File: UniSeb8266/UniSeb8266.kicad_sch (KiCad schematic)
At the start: 30 parts, among them IC1 WEMOS-D1-MINI, IC2 GY-BME280-3.3, IC3 LM1117IMPX-, IC4 MCP23008SS, IC5 RT9400, IC6 AMS5915, J1 22-?-0327-2031, X1 AK500/2, X2 AK500/2, X3 233-503, X5 233-504, X61 JST-XH-05-PIN-LONG-PAD, X7 0446200002, X8 233-508

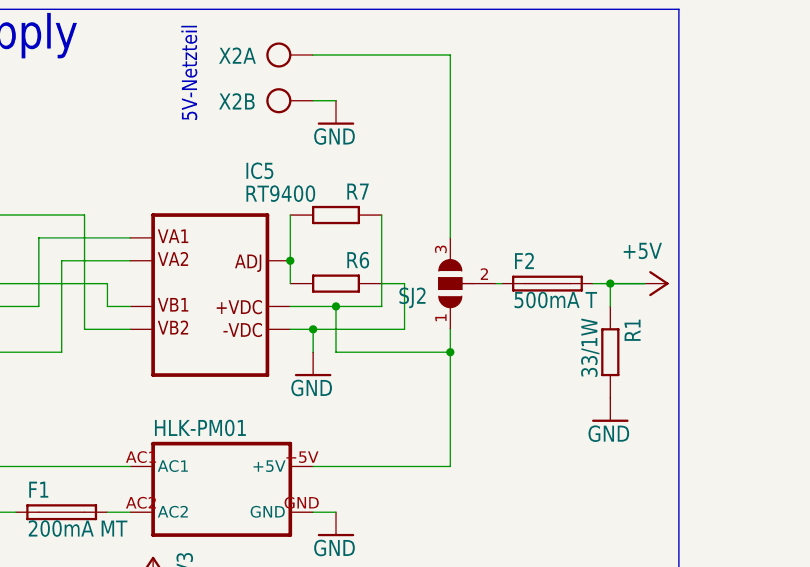
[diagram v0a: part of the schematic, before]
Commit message: changed name of SJ2 -> SJ1
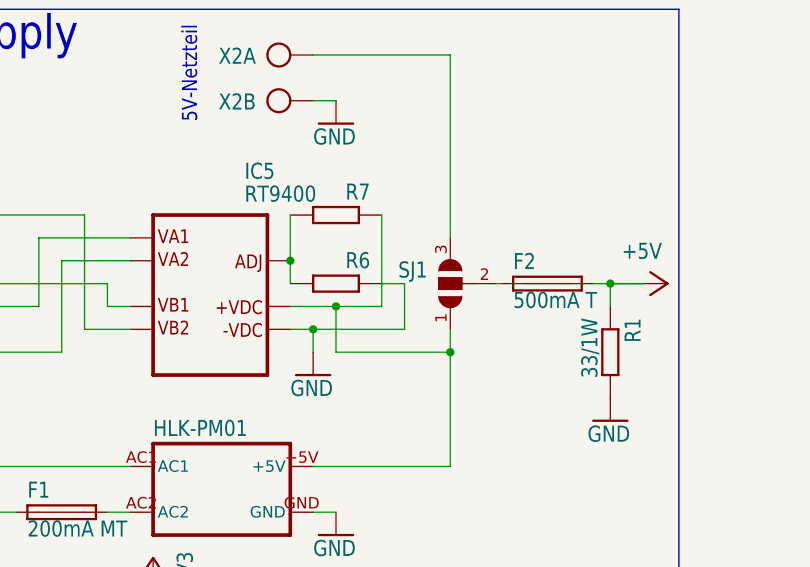
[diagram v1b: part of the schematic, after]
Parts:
- renumbered SJ2 to SJ1
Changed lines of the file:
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@@
   (symbol (lib_id "UniSeb8266-eagle-import:SJ2W") (at 96.52 53.34 180) (unit 1)
     (in_bom yes) (on_board yes) (dnp no)
-    (property "Reference" "SJ2" (at 93.98 53.721 0)
+    (property "Reference" "SJ1" (at 93.98 50.8 0)
       (effects (font (size 1.778 1.5113)) (justify left bottom))
     )
@@
       (project "UniSeb8266"
         (path "/7f528db3-ace1-4a57-b27a-eb0bf0e98f2a"
-          (reference "SJ2") (unit 1)
+          (reference "SJ1") (unit 1)
         )
       )

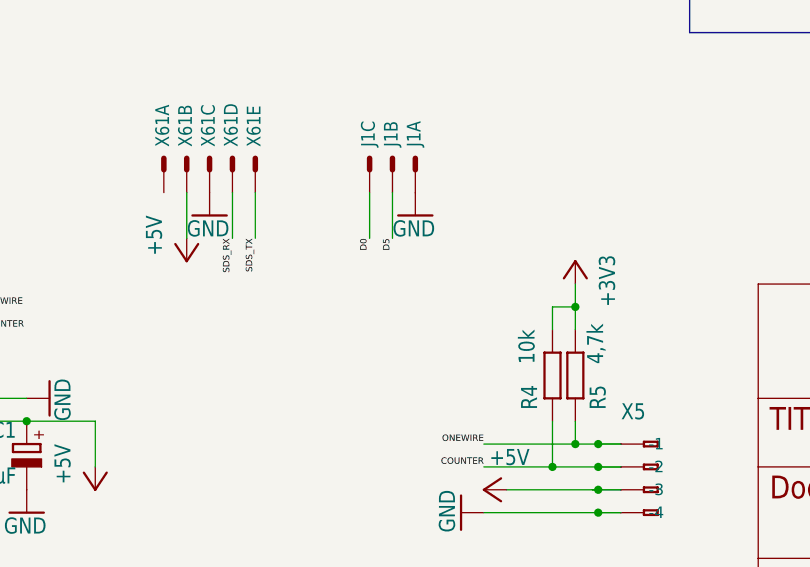
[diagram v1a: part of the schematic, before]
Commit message: added SJ2 to change pin-2 usage of "Molex KK 254" connector (3.3V or D5)
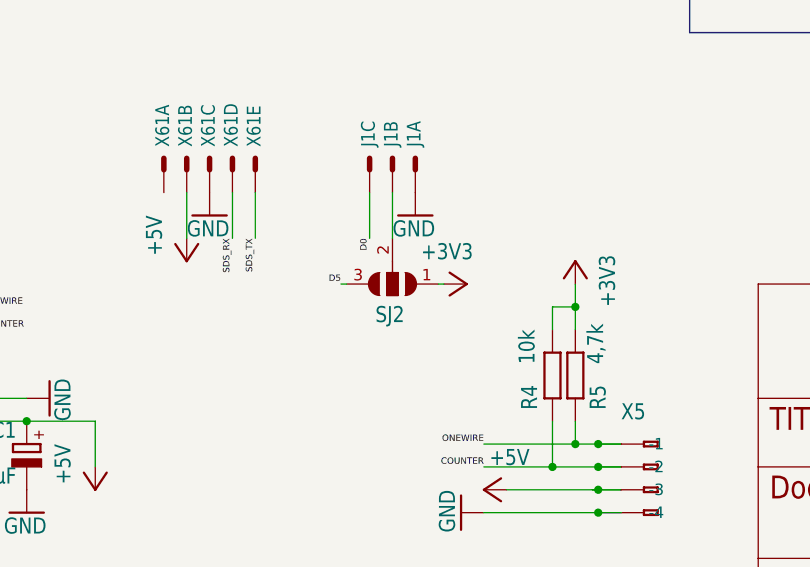
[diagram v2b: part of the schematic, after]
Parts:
- added SJ2: SJ2W, UniSeb8266:SJ_2, symbol UniSeb8266-eagle-import:SJ2W
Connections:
- net +3V3: now also SJ2.1
- net D5: now also SJ2.3; no longer J1.2 (S)
- new net: J1.2 (S), SJ2.2
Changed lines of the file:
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@@
     (stroke (width 0.1524) (type solid))
+  )
+  (wire (pts (xy 139.7 152.4) (xy 139.7 157.48))
+    (stroke (width 0) (type default))
   )
   (wire (pts (xy 157.48 177.8) (xy 157.48 182.88))
@@
     (stroke (width 0.1524) (type solid))
   )
+  (wire (pts (xy 133.985 162.56) (xy 134.62 162.56))
+    (stroke (width 0) (type default))
+  )
   (wire (pts (xy 81.28 33.02) (xy 83.82 33.02))
     (stroke (width 0.1524) (type solid))
@@
     (stroke (width 0.1524) (type solid))
   )
-  (wire (pts (xy 139.7 152.4) (xy 139.7 157.48))
-    (stroke (width 0.1524) (type solid))
-  )
   (wire (pts (xy 99.06 177.8) (xy 106.68 177.8))
     (stroke (width 0.1524) (type solid))
@@
   (wire (pts (xy 243.84 99.06) (xy 251.46 99.06))
     (stroke (width 0.1524) (type solid))
+  )
+  (wire (pts (xy 145.415 162.56) (xy 144.78 162.56))
+    (stroke (width 0) (type default))
   )
   (wire (pts (xy 220.98 71.12) (xy 220.98 66.04))
@@
     (effects (font (size 0.7112 0.7112)) (justify right bottom))
   )
-  (label "D5" (at 139.7 157.48 270) (fields_autoplaced)
+  (label "D5" (at 133.985 162.56 180) (fields_autoplaced)
     (effects (font (size 0.7112 0.7112)) (justify right bottom))
   )
@@
     )
   )
+  (symbol (lib_id "UniSeb8266-eagle-import:SJ2W") (at 139.7 162.56 270) (unit 1)
+    (in_bom yes) (on_board yes) (dnp no)
+    (property "Reference" "SJ2" (at 137.795 167.005 90)
+      (effects (font (size 1.778 1.5113)) (justify left bottom))
+    )
+    (property "Value" "SJ2W" (at 137.795 165.1 0)
+      (effects (font (size 1.778 1.5113)) (justify left bottom) hide)
+    )
+    (property "Footprint" "UniSeb8266:SJ_2" (at 139.7 162.56 0)
+      (effects (font (size 1.27 1.27)) hide)
+    )
+    (property "Datasheet" "" (at 139.7 162.56 0)
+      (effects (font (size 1.27 1.27)) hide)
+    )
+    (pin "1")
+    (pin "2")
+    (pin "3")
+    (instances
+      (project "UniSeb8266"
+        (path "/7f528db3-ace1-4a57-b27a-eb0bf0e98f2a"
+          (reference "SJ2") (unit 1)
+        )
+      )
+    )
+  )
   (symbol (lib_id "UniSeb8266-eagle-import:R-EU_R1206") (at 157.48 172.72 90) (unit 1)
     (in_bom yes) (on_board yes) (dnp no)
@@
         )
       )
+    )
+  )
+  (symbol (lib_id "UniSeb8266-eagle-import:+3V3") (at 147.955 162.56 270) (unit 1)
+    (in_bom yes) (on_board yes) (dnp no)
+    (property "Reference" "#+3V02" (at 147.955 162.56 0)
+      (effects (font (size 1.27 1.27)) hide)
+    )
+    (property "Value" "+3V3" (at 142.875 160.02 90)
+      (effects (font (size 1.778 1.5113)) (justify left bottom))
+    )
+    (property "Footprint" "" (at 147.955 162.56 0)
+      (effects (font (size 1.27 1.27)) hide)
+    )
+    (property "Datasheet" "" (at 147.955 162.56 0)
+      (effects (font (size 1.27 1.27)) hide)
+    )
+    (pin "1")
+    (instances
+      (project "UniSeb8266"
+        (path "/7f528db3-ace1-4a57-b27a-eb0bf0e98f2a"
+          (reference "#+3V02") (unit 1)
+        )
+      )

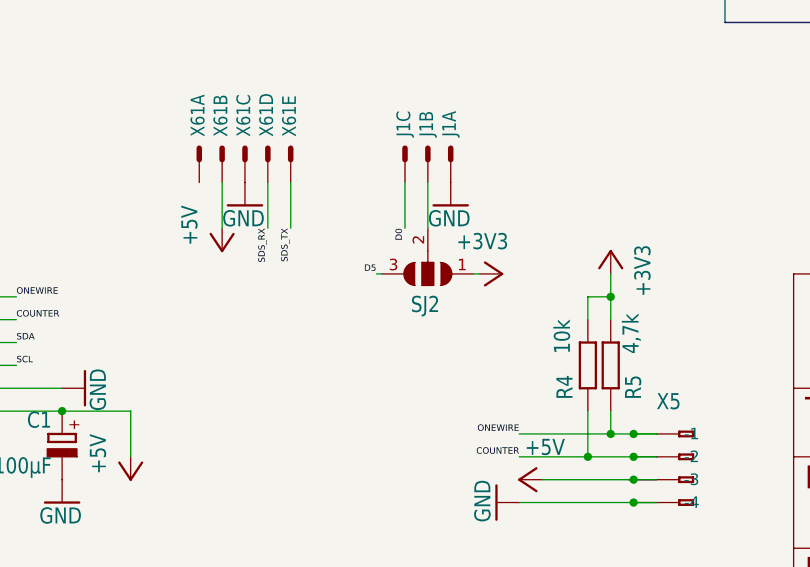
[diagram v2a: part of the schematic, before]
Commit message: added R2 pullup for pin3 of J1
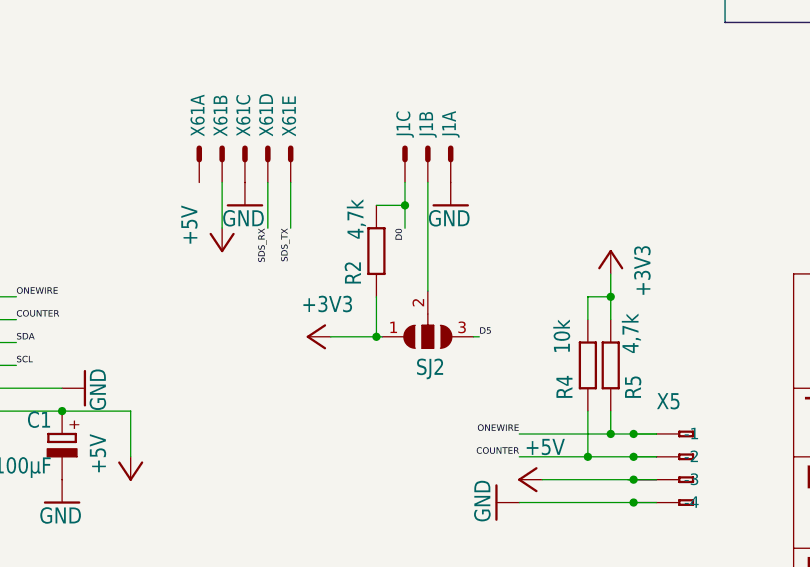
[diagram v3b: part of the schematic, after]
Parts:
- added R2: 4,7k, Resistor_SMD:R_0603_1608Metric, symbol UniSeb8266-eagle-import:R-EU_R1206
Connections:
- net +3V3: now also R2.1
- net D0: now also R2.2
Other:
- moved on the sheet: SJ2
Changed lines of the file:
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@@
   (junction (at 246.38 83.82) (diameter 0) (color 0 0 0 0)
   )
+  (junction (at 137.16 154.94) (diameter 0) (color 0 0 0 0)
+  )
   (junction (at 160.02 165.1) (diameter 0) (color 0 0 0 0)
   )
@@
   (junction (at 43.18 60.96) (diameter 0) (color 0 0 0 0)
   )
+  (junction (at 133.985 169.545) (diameter 0) (color 0 0 0 0)
+  )
   (junction (at 162.56 185.42) (diameter 0) (color 0 0 0 0)
   )
@@
     (stroke (width 0.1524) (type solid))
   )
-  (wire (pts (xy 137.16 152.4) (xy 137.16 157.48))
+  (wire (pts (xy 137.16 152.4) (xy 137.16 154.94))
     (stroke (width 0.1524) (type solid))
   )
@@
     (stroke (width 0.1524) (type solid))
   )
+  (wire (pts (xy 137.16 154.94) (xy 137.16 157.48))
+    (stroke (width 0.1524) (type solid))
+  )
   (wire (pts (xy 152.4 185.42) (xy 162.56 185.42))
     (stroke (width 0.1524) (type solid))
@@
     (stroke (width 0.1524) (type solid))
   )
+  (wire (pts (xy 133.985 154.94) (xy 137.16 154.94))
+    (stroke (width 0) (type default))
+  )
   (wire (pts (xy 256.54 53.34) (xy 256.54 50.8))
     (stroke (width 0.1524) (type solid))
@@
     (stroke (width 0.1524) (type solid))
   )
-  (wire (pts (xy 139.7 152.4) (xy 139.7 157.48))
+  (wire (pts (xy 139.7 152.4) (xy 139.7 164.465))
     (stroke (width 0) (type default))
   )
@@
     (stroke (width 0.1524) (type solid))
   )
+  (wire (pts (xy 133.985 169.545) (xy 134.62 169.545))
+    (stroke (width 0) (type default))
+  )
   (wire (pts (xy 243.84 93.98) (xy 256.54 93.98))
     (stroke (width 0.1524) (type solid))
@@
     (stroke (width 0.1524) (type solid))
   )
-  (wire (pts (xy 133.985 162.56) (xy 134.62 162.56))
+  (wire (pts (xy 145.415 169.545) (xy 144.78 169.545))
     (stroke (width 0) (type default))
   )
@@
     (stroke (width 0.1524) (type solid))
   )
+  (wire (pts (xy 133.985 165.1) (xy 133.985 169.545))
+    (stroke (width 0) (type default))
+  )
   (wire (pts (xy 43.18 60.96) (xy 53.34 60.96))
     (stroke (width 0.1524) (type solid))
@@
     (stroke (width 0.1524) (type solid))
   )
-  (wire (pts (xy 145.415 162.56) (xy 144.78 162.56))
+  (wire (pts (xy 128.905 169.545) (xy 133.985 169.545))
     (stroke (width 0) (type default))
   )
@@
     (effects (font (size 0.7112 0.7112)) (justify right bottom))
   )
-  (label "D5" (at 133.985 162.56 180) (fields_autoplaced)
-    (effects (font (size 0.7112 0.7112)) (justify right bottom))
+  (label "D5" (at 145.415 169.545 0) (fields_autoplaced)
+    (effects (font (size 0.7112 0.7112)) (justify left bottom))
   )
   (label "EXP-INT" (at 53.34 170.18 180) (fields_autoplaced)
@@
     )
   )
-  (symbol (lib_id "UniSeb8266-eagle-import:SJ2W") (at 139.7 162.56 270) (unit 1)
-    (in_bom yes) (on_board yes) (dnp no)
-    (property "Reference" "SJ2" (at 137.795 167.005 90)
-      (effects (font (size 1.778 1.5113)) (justify left bottom))
-    )
-    (property "Value" "SJ2W" (at 137.795 165.1 0)
+  (symbol (lib_id "UniSeb8266-eagle-import:SJ2W") (at 139.7 169.545 90) (mirror x) (unit 1)
+    (in_bom yes) (on_board yes) (dnp no)
+    (property "Reference" "SJ2" (at 141.605 173.99 90)
+      (effects (font (size 1.778 1.5113)) (justify left bottom))
+    )
+    (property "Value" "SJ2W" (at 141.605 172.085 0)
       (effects (font (size 1.778 1.5113)) (justify left bottom) hide)
     )
-    (property "Footprint" "UniSeb8266:SJ_2" (at 139.7 162.56 0)
-      (effects (font (size 1.27 1.27)) hide)
-    )
-    (property "Datasheet" "" (at 139.7 162.56 0)
+    (property "Footprint" "UniSeb8266:SJ_2" (at 139.7 169.545 0)
+      (effects (font (size 1.27 1.27)) hide)
+    )
+    (property "Datasheet" "" (at 139.7 169.545 0)
       (effects (font (size 1.27 1.27)) hide)
     )
@@
     )
   )
-  (symbol (lib_id "UniSeb8266-eagle-import:+3V3") (at 147.955 162.56 270) (unit 1)
-    (in_bom yes) (on_board yes) (dnp no)
-    (property "Reference" "#+3V02" (at 147.955 162.56 0)
-      (effects (font (size 1.27 1.27)) hide)
-    )
-    (property "Value" "+3V3" (at 142.875 160.02 90)
-      (effects (font (size 1.778 1.5113)) (justify left bottom))
-    )
-    (property "Footprint" "" (at 147.955 162.56 0)
-      (effects (font (size 1.27 1.27)) hide)
-    )
-    (property "Datasheet" "" (at 147.955 162.56 0)
+  (symbol (lib_id "UniSeb8266-eagle-import:+3V3") (at 126.365 169.545 90) (mirror x) (unit 1)
+    (in_bom yes) (on_board yes) (dnp no)
+    (property "Reference" "#+3V02" (at 126.365 169.545 0)
+      (effects (font (size 1.27 1.27)) hide)
+    )
+    (property "Value" "+3V3" (at 131.445 167.005 90)
+      (effects (font (size 1.778 1.5113)) (justify left bottom))
+    )
+    (property "Footprint" "" (at 126.365 169.545 0)
+      (effects (font (size 1.27 1.27)) hide)
+    )
+    (property "Datasheet" "" (at 126.365 169.545 0)
       (effects (font (size 1.27 1.27)) hide)
     )
@@
         )
       )
+    )
+  )
+  (symbol (lib_id "UniSeb8266-eagle-import:R-EU_R1206") (at 133.985 160.02 270) (mirror x) (unit 1)
+    (in_bom yes) (on_board yes) (dnp no)
+    (property "Reference" "R2" (at 130.4036 163.83 0)
+      (effects (font (size 1.778 1.5113)) (justify left bottom))
+    )
+    (property "Value" "4,7k" (at 130.683 158.75 0)
+      (effects (font (size 1.778 1.5113)) (justify left bottom))
+    )
+    (property "Footprint" "Resistor_SMD:R_0603_1608Metric" (at 133.985 160.02 0)
+      (effects (font (size 1.27 1.27)) hide)
+    )
+    (property "Datasheet" "" (at 133.985 160.02 0)
+      (effects (font (size 1.27 1.27)) hide)
+    )
+    (property "LCSC" "C23162" (at 133.985 160.02 0)
+      (effects (font (size 1.27 1.27)) hide)
+    )
+    (pin "1")
+    (pin "2")
+    (instances
+      (project "UniSeb8266"
+        (path "/7f528db3-ace1-4a57-b27a-eb0bf0e98f2a"
+          (reference "R2") (unit 1)
+        )
+      )
